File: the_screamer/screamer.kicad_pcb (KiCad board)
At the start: 4 copper layers, 18 x 14 mm, 15 parts, among them U1 TC2185-3.3VxCTTR, U2 MAX2606

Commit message: Added Timer power connector
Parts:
- added J1: Conn_01x02_Pin, Connector_PinHeader_2.00mm:PinHeader_1x02_P2.00mm_Vertical, B.Cu at (166.5, 93.0)
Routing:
- net Net-(BT1--): track 6.11 -> 15.4 mm
- net Net-(BT1-+): track 6.11 -> 11.9 mm

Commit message: Added resistor values to the voltage divider
The resistors are 681 ohms and 1.2k ohms. I also adjusted some stuff on the silkscreen to make it more readable.
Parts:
- R1: value R -> 1.2k
- R2: value R -> 681
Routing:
- net GND: track 21.9 -> 23.7 mm
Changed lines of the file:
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@@
 		(tags "1775469-2 ")
 		(property "Reference" "BT1"
-			(at -0.01435 -2.9138 0)
+			(at -0.01435 -5.4138 0)
 			(unlocked yes)
 			(layer "F.SilkS")
@@
 			)
 		)
-		(property "Value" "R"
-			(at 0 8.5 0)
+		(property "Value" "681"
+			(at 0 -8.5 0)
 			(layer "F.Fab")
 			(effects
@@
 		(tags "Through hole pin header THT 1x02 2.54mm single row")
 		(property "Reference" "AE1"
-			(at 2.474874 1.275 315)
+			(at 2.474874 1.275 -45)
 			(layer "F.SilkS")
 			(effects
@@
 			)
 		)
-		(property "Value" "R"
+		(property "Value" "1.2k"
 			(at 0 8.5 180)
 			(layer "F.Fab")
@@
 		)
 		(property "Value" "Conn_01x02_Pin"
-			(at 0 -4.06 270)
+			(at 0 2.5 90)
 			(layer "B.Fab")
 			(effects
@@
 		)
 		(fp_text user "${REFERENCE}"
-			(at 0 -1 360)
+			(at 0 -1 0)
 			(layer "B.Fab")
 			(effects
@@
 	)
 	(segment
-		(start 154 90.6375)
-		(end 154 92)
-		(width 0.5)
+		(start 160.265 92.43)
+		(end 162.07 92.43)
+		(width 0.75)
 		(layer "B.Cu")
 		(net 4)
@@
 		(start 158.9125 90.6375)
 		(end 158.9125 91.9125)
-		(width 0.25)
+		(width 0.75)
 		(layer "B.Cu")
 		(net 4)
 	)
 	(segment
-		(start 159.43 92.43)
-		(end 160.265 92.43)
-		(width 0.25)
+		(start 158.9125 91.9125)
+		(end 159.43 92.43)
+		(width 0.75)
 		(layer "B.Cu")
 		(net 4)
 	)
 	(segment
-		(start 158.9125 91.9125)
-		(end 159.43 92.43)
-		(width 0.25)
+		(start 154 90.6375)
+		(end 154 92)
+		(width 0.5)
+		(layer "B.Cu")
+		(net 4)
+	)
+	(segment
+		(start 159.43 92.43)
+		(end 160.265 92.43)
+		(width 0.75)
 		(layer "B.Cu")
 		(net 4)
@@
 	)
 	(segment
-		(start 157.98565 92.5862)
-		(end 157.98565 94.98565)
+		(start 157.98565 95.48565)
+		(end 158 95.5)
 		(width 0.75)
 		(layer "F.Cu")
@@
 	)
 	(segment
-		(start 157.98565 94.98565)
-		(end 158 95)
-		(width 0.25)
+		(start 157.98565 92.5862)
+		(end 157.98565 95.48565)
+		(width 0.75)
 		(layer "F.Cu")
 		(net 8)
 	)
 	(via
-		(at 158 95)
+		(at 158 95.5)
 		(size 0.6)
 		(drill 0.3)
@@
 	)
 	(segment
-		(start 158 95)
-		(end 159 94)
+		(start 159.25 94.25)
+		(end 165.25 94.25)
 		(width 0.75)
 		(layer "B.Cu")
@@
 	)
 	(segment
-		(start 159 94)
-		(end 165.5 94)
+		(start 158 95.5)
+		(end 159.25 94.25)
 		(width 0.75)
 		(layer "B.Cu")
@@
 	)
 	(segment
-		(start 165.5 94)
-		(end 166.5 93)
+		(start 157.725 95.775)
+		(end 158 95.5)
 		(width 0.75)
 		(layer "B.Cu")
@@
 	)
 	(segment
-		(start 157.725 95.275)
-		(end 158 95)
+		(start 165.25 94.25)
+		(end 166.5 93)
 		(width 0.75)
 		(layer "B.Cu")
@@
 	(segment
 		(start 157.725 98.58)
-		(end 157.725 95.275)
+		(end 157.725 95.775)
 		(width 0.75)
 		(layer "B.Cu")
@@
 	)
 	(segment
-		(start 159.985651 92.5862)
-		(end 159.985651 94.985651)
+		(start 159.985651 95.485651)
+		(end 160 95.5)
 		(width 0.75)
 		(layer "F.Cu")
@@
 	)
 	(segment
-		(start 159.985651 94.985651)
-		(end 160 95)
-		(width 0.25)
-		(layer "F.Cu")
-		(net 9)
-	)
-	(segment
 		(start 162 95.5)
 		(end 164.5 93)
@@
 	)
 	(segment
-		(start 159.985651 94.985651)
-		(end 160.5 95.5)
+		(start 159.985651 92.5862)
+		(end 159.985651 95.485651)
 		(width 0.75)
 		(layer "F.Cu")
@@
 	)
 	(segment
-		(start 160.5 95.5)
+		(start 160 95.5)
 		(end 162 95.5)
 		(width 0.75)
@@
 	)
 	(via
-		(at 160 95)
+		(at 160 95.5)
 		(size 0.6)
 		(drill 0.3)
@@
 	)
 	(segment
-		(start 160.265 98.58)
-		(end 160.265 95.265)
+		(start 160.265 95.765)
+		(end 160 95.5)
 		(width 0.75)
 		(layer "B.Cu")
@@
 	)
 	(segment
-		(start 160.265 95.265)
-		(end 160 95)
+		(start 160.265 98.58)
+		(end 160.265 95.765)
 		(width 0.75)
 		(layer "B.Cu")

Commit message: Revert "Merge branch 'main' of https://github.com/CSM-Rocketry-Club/flight-computers"
This reverts commit 3edd037536e7f8eb1c97200e83282850b3e66c85, reversing
changes made to 45bb795bdd8a498dcdd2092ff2f1a03ff2b1d69a.
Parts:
- R1: value 1.2k -> R
- R2: value 681 -> R
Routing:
- net GND: track 23.7 -> 21.9 mm
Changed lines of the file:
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@@
 		(tags "1775469-2 ")
 		(property "Reference" "BT1"
-			(at -0.01435 -5.4138 0)
+			(at -0.01435 -2.9138 0)
 			(unlocked yes)
 			(layer "F.SilkS")
@@
 			)
 		)
-		(property "Value" "681"
-			(at 0 -8.5 0)
+		(property "Value" "R"
+			(at 0 8.5 0)
 			(layer "F.Fab")
 			(effects
@@
 		(tags "Through hole pin header THT 1x02 2.54mm single row")
 		(property "Reference" "AE1"
-			(at 2.474874 1.275 -45)
+			(at 2.474874 1.275 315)
 			(layer "F.SilkS")
 			(effects
@@
 			)
 		)
-		(property "Value" "1.2k"
+		(property "Value" "R"
 			(at 0 8.5 180)
 			(layer "F.Fab")
@@
 		)
 		(property "Value" "Conn_01x02_Pin"
-			(at 0 2.5 90)
+			(at 0 -4.06 270)
 			(layer "B.Fab")
 			(effects
@@
 		)
 		(fp_text user "${REFERENCE}"
-			(at 0 -1 0)
+			(at 0 -1 360)
 			(layer "B.Fab")
 			(effects
@@
 	)
 	(segment
-		(start 160.265 92.43)
-		(end 162.07 92.43)
-		(width 0.75)
+		(start 154 90.6375)
+		(end 154 92)
+		(width 0.5)
 		(layer "B.Cu")
 		(net 4)
@@
 		(start 158.9125 90.6375)
 		(end 158.9125 91.9125)
-		(width 0.75)
-		(layer "B.Cu")
-		(net 4)
-	)
-	(segment
-		(start 158.9125 91.9125)
-		(end 159.43 92.43)
-		(width 0.75)
+		(width 0.25)
 		(layer "B.Cu")
 		(net 4)
 	)
 	(segment
-		(start 154 90.6375)
-		(end 154 92)
-		(width 0.5)
+		(start 159.43 92.43)
+		(end 160.265 92.43)
+		(width 0.25)
 		(layer "B.Cu")
 		(net 4)
 	)
 	(segment
-		(start 159.43 92.43)
-		(end 160.265 92.43)
-		(width 0.75)
+		(start 158.9125 91.9125)
+		(end 159.43 92.43)
+		(width 0.25)
 		(layer "B.Cu")
 		(net 4)
@@
 	)
 	(segment
-		(start 157.98565 95.48565)
-		(end 158 95.5)
+		(start 157.98565 92.5862)
+		(end 157.98565 94.98565)
 		(width 0.75)
 		(layer "F.Cu")
@@
 	)
 	(segment
-		(start 157.98565 92.5862)
-		(end 157.98565 95.48565)
-		(width 0.75)
+		(start 157.98565 94.98565)
+		(end 158 95)
+		(width 0.25)
 		(layer "F.Cu")
 		(net 8)
 	)
 	(via
-		(at 158 95.5)
+		(at 158 95)
 		(size 0.6)
 		(drill 0.3)
@@
 	)
 	(segment
-		(start 159.25 94.25)
-		(end 165.25 94.25)
+		(start 158 95)
+		(end 159 94)
 		(width 0.75)
 		(layer "B.Cu")
@@
 	)
 	(segment
-		(start 158 95.5)
-		(end 159.25 94.25)
+		(start 159 94)
+		(end 165.5 94)
 		(width 0.75)
 		(layer "B.Cu")
@@
 	)
 	(segment
-		(start 157.725 95.775)
-		(end 158 95.5)
+		(start 165.5 94)
+		(end 166.5 93)
 		(width 0.75)
 		(layer "B.Cu")
@@
 	)
 	(segment
-		(start 165.25 94.25)
-		(end 166.5 93)
+		(start 157.725 95.275)
+		(end 158 95)
 		(width 0.75)
 		(layer "B.Cu")
@@
 	(segment
 		(start 157.725 98.58)
-		(end 157.725 95.775)
+		(end 157.725 95.275)
 		(width 0.75)
 		(layer "B.Cu")
@@
 	)
 	(segment
-		(start 159.985651 95.485651)
-		(end 160 95.5)
+		(start 159.985651 92.5862)
+		(end 159.985651 94.985651)
 		(width 0.75)
 		(layer "F.Cu")
@@
 	)
 	(segment
+		(start 159.985651 94.985651)
+		(end 160 95)
+		(width 0.25)
+		(layer "F.Cu")
+		(net 9)
+	)
+	(segment
 		(start 162 95.5)
 		(end 164.5 93)
@@
 	)
 	(segment
-		(start 159.985651 92.5862)
-		(end 159.985651 95.485651)
+		(start 159.985651 94.985651)
+		(end 160.5 95.5)
 		(width 0.75)
 		(layer "F.Cu")
@@
 	)
 	(segment
-		(start 160 95.5)
+		(start 160.5 95.5)
 		(end 162 95.5)
 		(width 0.75)
@@
 	)
 	(via
-		(at 160 95.5)
+		(at 160 95)
 		(size 0.6)
 		(drill 0.3)
@@
 	)
 	(segment
-		(start 160.265 95.765)
-		(end 160 95.5)
+		(start 160.265 98.58)
+		(end 160.265 95.265)
 		(width 0.75)
 		(layer "B.Cu")
@@
 	)
 	(segment
-		(start 160.265 98.58)
-		(end 160.265 95.765)
+		(start 160.265 95.265)
+		(end 160 95)
 		(width 0.75)
 		(layer "B.Cu")

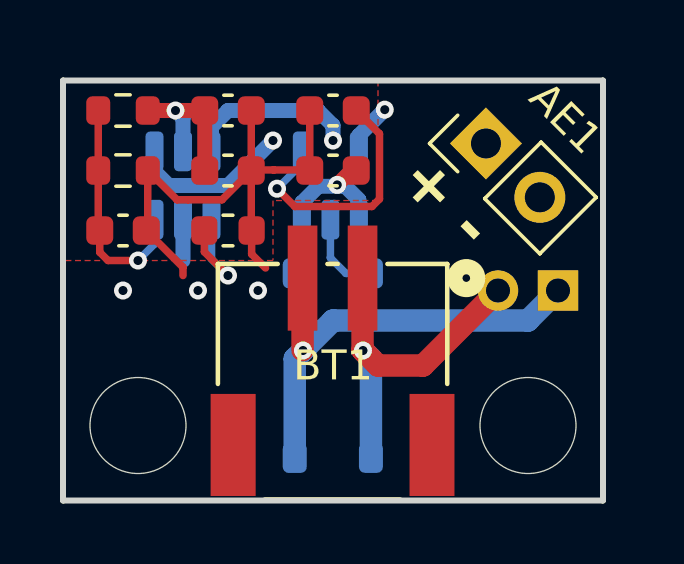
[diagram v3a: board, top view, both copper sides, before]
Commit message: Updated Screamer to V0.0.3
Swapped VCO to MAX2623, adjusted filtering capacitors, and rerouted board.
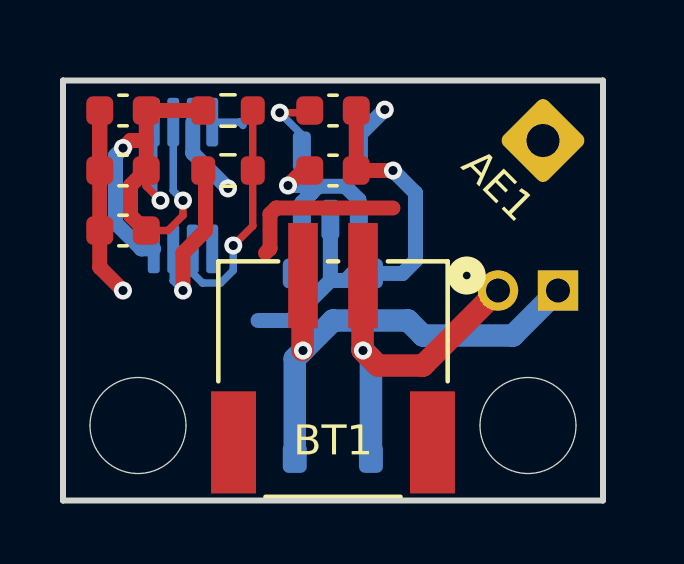
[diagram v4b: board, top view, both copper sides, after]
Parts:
- removed the C2 at (155.5, 87.0)
- removed L1: 13n, Inductor_SMD:L_0603_1608Metric
- added C3: 1u, Capacitor_SMD:C_0603_1608Metric, F.Cu at (152.0, 87.0)
- AE1: footprint Connector_PinHeader_2.54mm:PinHeader_1x02_P2.54mm_Vertical -> Connector_Wire:SolderWire-0.5sqmm_1x01_D0.9mm_OD2.1mm
- BT1: footprint locals but working PLEASE:JST_CONN2_1775469-2_TEC -> locals_but_working_PLEASE:CONN2_1775469-2_TEC
- C4, C5: value 0.01u -> 220p
- R1: value R -> 1.2k
- R2: value R -> 750
- U2: value MAX2606 -> MAX2623EUA+T; footprint Package_TO_SOT_SMD:SOT-23-6 -> Package_SO:MSOP-8_3x3mm_P0.65mm
- moved C4 3.50 mm to (152.0, 89.0), turned to 180 degrees
- moved R1 3.50 mm to (155.5, 87.0), turned to 0 degrees
- moved R2 3.50 mm to (155.5, 89.0), turned to 180 degrees
- moved AE1 1.90 mm to (166.0, 88.0), turned to -45 degrees
- moved BT1 0.99 mm to (158.0, 92.5)
- turned C1 to 0 degrees
- turned C2 to 0 degrees
- renumbered C3 to C2
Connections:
- AE1 pad 1: /RF+ -> RF_OUT
- C4 pad 1: V_{CC} -> VCC
- C5 pad 1: GND -> VCC
- C5 pad 2: Net-(U2-TUNE) -> GND
- R1 pad 1: V_{CC} -> VCC
- R1 pad 2: Net-(U2-TUNE) -> V_{TUNE}
- R2 pad 1: Net-(U2-TUNE) -> V_{TUNE}
- U1 pad 5: V_{CC} -> VCC
- U2 pad 1: Net-(U2-IND) -> unconnected-(U2-NC-Pad1)
- U2 pad 2: GND -> V_{TUNE}
- U2 pad 3: Net-(U2-TUNE) -> GND
- U2 pad 4: /RF+ -> VCC
- U2 pad 5: V_{CC} -> VCC
- U2 pad 6: /RF- -> VCC
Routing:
- net VCC: track 0.00 -> 21.8 mm, vias 0 -> 4
- net RF_OUT: track 0.00 -> 14.4 mm, vias 0 -> 1
- net /RF-: track 14.0 -> 0.00 mm, vias 1 -> 0
- net GND: track 21.9 -> 35.6 mm
- net /RF+: track 13.2 -> 0.00 mm, vias 1 -> 0
- net V_{TUNE}: track 0.00 -> 8.07 mm, vias 0 -> 1
- net Net-(U2-TUNE): track 7.72 -> 0.00 mm, vias 1 -> 0
- net V_{CC}: track 7.11 -> 0.00 mm, vias 2 -> 0
- net Net-(U1-BP): track 8.62 -> 2.63 mm
- net Net-(U2-IND): track 3.92 -> 0.00 mm, vias 1 -> 0
- net V_{B}: track 6.38 -> 7.24 mm
- added copper zone on In1.Cu, net VCC
- removed copper zone on In1.Cu, net V_{CC}
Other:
- board text added: "V0.0.3"
- board text removed: "+ -"
- board text removed: "V0.0.1"
